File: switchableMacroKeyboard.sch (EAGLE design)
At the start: 36 parts

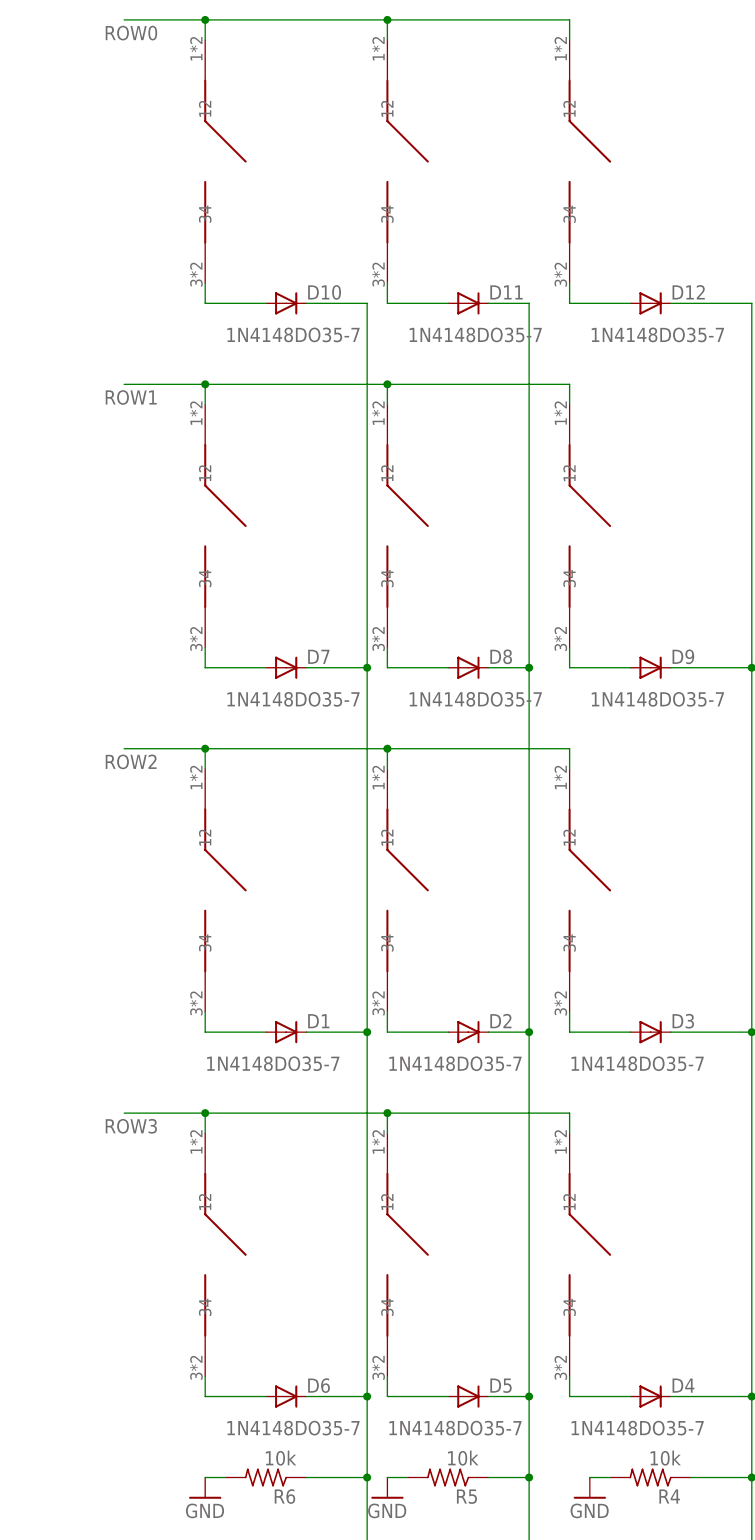
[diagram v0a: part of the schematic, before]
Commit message: Switched the buttons to Cherry MX Blues, but found this may require a bigger board, mostly length-wise. Moving the diodes out of the way of the key has cramped things. To do: adjust board dimensions to fit new buttons, reroute keypad traces.
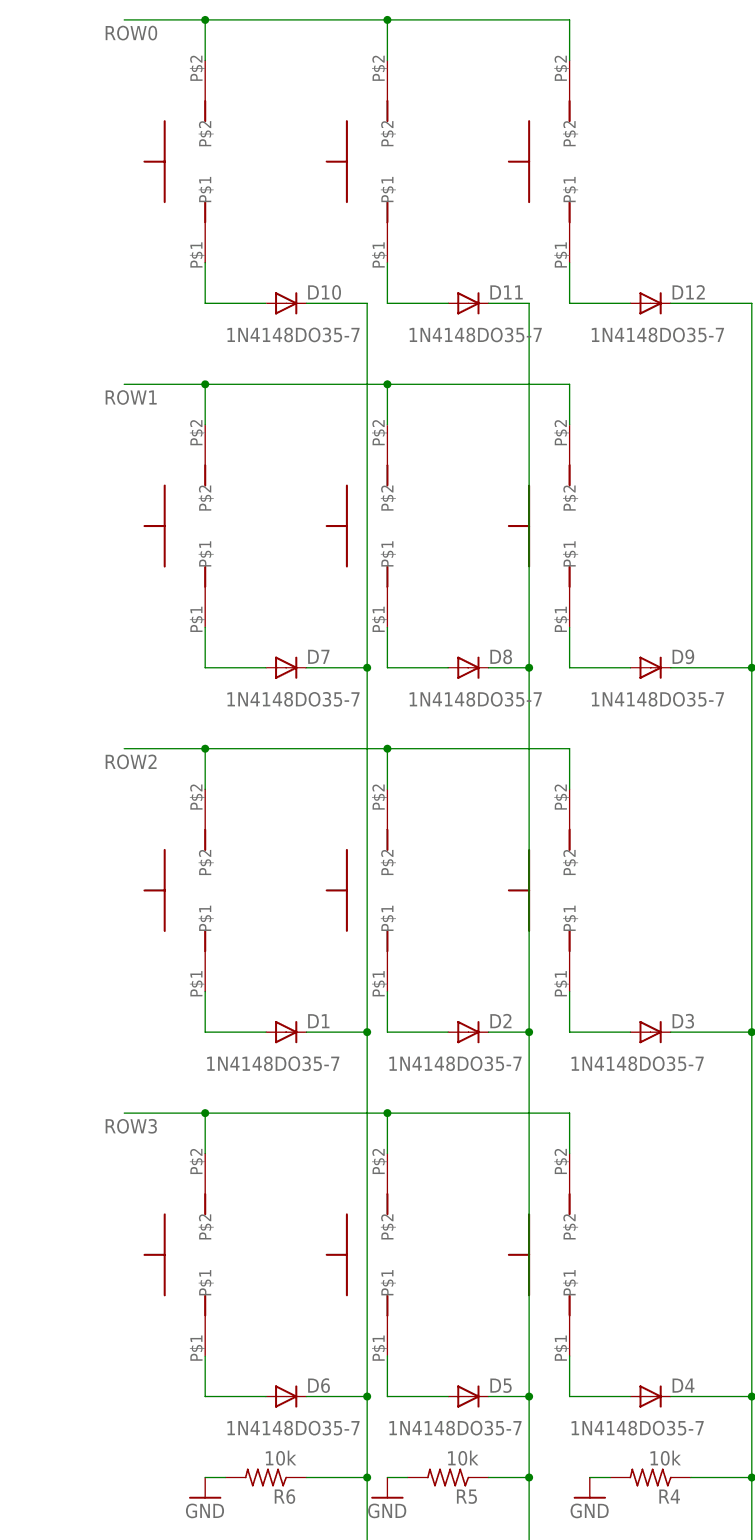
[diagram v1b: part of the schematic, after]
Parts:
- removed 00, 01, 02, 10, 11, 12, 20, 21, 22, 30, 31, 32: TACT-PTS526-SMG15-SMTR2-LFS, ARNEInput:TACT-PTS526-SMG15-SMTR2-LFS
- added U$10, U$11, U$12, U$14, U$15, U$16, U$4, U$5, U$6, U$7, U$8, U$9: CHERRYMXBLUE, ARNEInput:CHERRYMXBLUE
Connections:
- net N$18: now also U$7.P$1; no longer 10.34
- net N$19: now also U$8.P$1; no longer 11.34
- net N$20: now also U$9.P$1; no longer 12.34
- net N$25: now also U$4.P$1; no longer 00.34
- net N$26: now also U$5.P$1; no longer 01.34
- net N$27: now also U$6.P$1; no longer 02.34
- net N$3: now also U$10.P$1; no longer 20.34
- net N$4: now also U$11.P$1; no longer 21.34
- net N$5: now also U$12.P$1; no longer 22.34
- net N$6: now also U$14.P$1; no longer 30.34
- net N$7: now also U$15.P$1; no longer 31.34
- net N$8: now also U$16.P$1; no longer 32.34
- net ROW0: now also U$4.P$2, U$5.P$2, U$6.P$2; no longer 00.12, 01.12, 02.12
- net ROW1: now also U$7.P$2, U$8.P$2, U$9.P$2; no longer 10.12, 11.12, 12.12
- net ROW2: now also U$10.P$2, U$11.P$2, U$12.P$2; no longer 20.12, 21.12, 22.12
- net ROW3: now also U$14.P$2, U$15.P$2, U$16.P$2; no longer 30.12, 31.12, 32.12

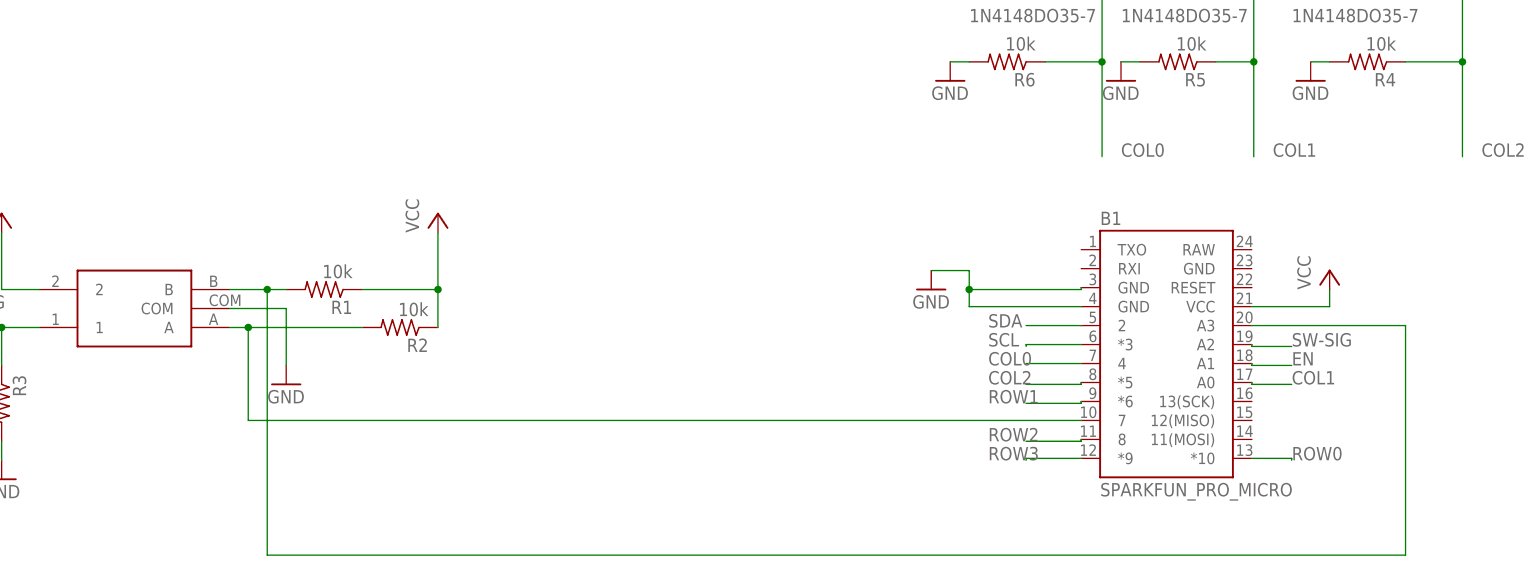
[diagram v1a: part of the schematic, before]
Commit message: Adjusted the size of the board and rerouted.
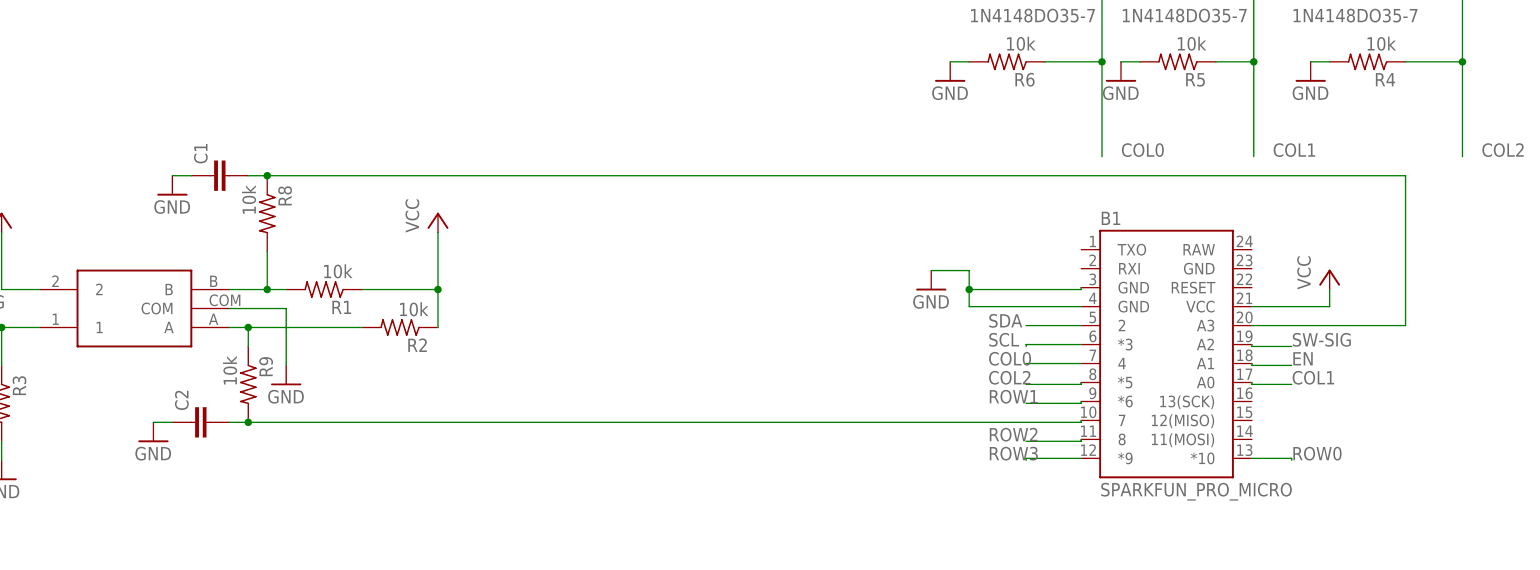
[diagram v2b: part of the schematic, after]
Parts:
- added C1, C2: (no value), capacitor-wima:C5/2.5
- added R8, R9: 10k, rcl:R-US_0207/10
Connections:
- new net N$10: R2.2, R9.1, U$13.A
- new net N$2: R1.2, R8.2, U$13.B
- net GND: now also C1.1, C2.1
- net N$1: now also C2.2, R9.2; no longer R2.2, U$13.A
- net N$9: now also C1.2, R8.1; no longer R1.2, U$13.B
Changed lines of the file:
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@@
 <part name="U$15" library="ARNEInput" deviceset="CHERRYMXBLUE" device=""/>
 <part name="U$16" library="ARNEInput" deviceset="CHERRYMXBLUE" device=""/>
+<part name="R8" library="rcl" library_urn="urn:adsk.eagle:library:334" deviceset="R-US_" device="0207/10" package3d_urn="urn:adsk.eagle:package:23491/2" value="10k"/>
+<part name="R9" library="rcl" library_urn="urn:adsk.eagle:library:334" deviceset="R-US_" device="0207/10" package3d_urn="urn:adsk.eagle:package:23491/2" value="10k"/>
+<part name="C1" library="capacitor-wima" library_urn="urn:adsk.eagle:library:116" deviceset="C" device="5/2.5" package3d_urn="urn:adsk.eagle:package:5426/1"/>
+<part name="C2" library="capacitor-wima" library_urn="urn:adsk.eagle:library:116" deviceset="C" device="5/2.5" package3d_urn="urn:adsk.eagle:package:5426/1"/>
+<part name="GND9" library="supply1" library_urn="urn:adsk.eagle:library:371" deviceset="GND" device=""/>
+<part name="GND10" library="supply1" library_urn="urn:adsk.eagle:library:371" deviceset="GND" device=""/>
 </parts>
 <sheets>
@@
 <instance part="U$15" gate="G$1" x="25.4" y="40.64" smashed="yes" rot="R90"/>
 <instance part="U$16" gate="G$1" x="48.26" y="40.64" smashed="yes" rot="R90"/>
+<instance part="R8" gate="G$1" x="-88.9" y="-7.62" smashed="yes" rot="R270">
+<attribute name="NAME" x="-87.4014" y="-3.81" size="1.778" layer="95" rot="R270"/>
+<attribute name="VALUE" x="-92.202" y="-3.81" size="1.778" layer="96" rot="R270"/>
+</instance>
+<instance part="R9" gate="G$1" x="-91.44" y="-30.48" smashed="yes" rot="R270">
+<attribute name="NAME" x="-89.9414" y="-26.67" size="1.778" layer="95" rot="R270"/>
+<attribute name="VALUE" x="-94.742" y="-26.67" size="1.778" layer="96" rot="R270"/>
+</instance>
+<instance part="C1" gate="G$1" x="-96.52" y="-2.54" smashed="yes" rot="R90">
+<attribute name="NAME" x="-96.901" y="-1.016" size="1.778" layer="95" rot="R90"/>
+<attribute name="VALUE" x="-91.821" y="-1.016" size="1.778" layer="96" rot="R90"/>
+</instance>
+<instance part="C2" gate="G$1" x="-99.06" y="-35.56" smashed="yes" rot="R90">
+<attribute name="NAME" x="-99.441" y="-34.036" size="1.778" layer="95" rot="R90"/>
+<attribute name="VALUE" x="-94.361" y="-34.036" size="1.778" layer="96" rot="R90"/>
+</instance>
+<instance part="GND9" gate="1" x="-104.14" y="-38.1" smashed="yes">
+<attribute name="VALUE" x="-106.68" y="-40.64" size="1.778" layer="96"/>
+</instance>
+<instance part="GND10" gate="1" x="-101.6" y="-5.08" smashed="yes">
+<attribute name="VALUE" x="-104.14" y="-7.62" size="1.778" layer="96"/>
+</instance>
 </instances>
 <busses>
@@
 <net name="N$9" class="0">
 <segment>
-<pinref part="R1" gate="G$1" pin="2"/>
-<pinref part="U$13" gate="G$1" pin="B"/>
-<wire x1="-86.36" y1="-17.78" x2="-88.9" y2="-17.78" width="0.1524" layer="91"/>
 <pinref part="B1" gate="G$1" pin="A3"/>
-<wire x1="-88.9" y1="-17.78" x2="-93.98" y2="-17.78" width="0.1524" layer="91"/>
 <wire x1="42.926" y1="-22.606" x2="63.5" y2="-22.606" width="0.1524" layer="91"/>
-<wire x1="63.5" y1="-22.606" x2="63.5" y2="-53.34" width="0.1524" layer="91"/>
-<wire x1="63.5" y1="-53.34" x2="-88.9" y2="-53.34" width="0.1524" layer="91"/>
-<wire x1="-88.9" y1="-53.34" x2="-88.9" y2="-17.78" width="0.1524" layer="91"/>
-<junction x="-88.9" y="-17.78"/>
+<wire x1="63.5" y1="-22.606" x2="63.5" y2="-2.54" width="0.1524" layer="91"/>
+<wire x1="63.5" y1="-2.54" x2="-88.9" y2="-2.54" width="0.1524" layer="91"/>
+<pinref part="R8" gate="G$1" pin="1"/>
+<pinref part="C1" gate="G$1" pin="2"/>
+<wire x1="-88.9" y1="-2.54" x2="-91.44" y2="-2.54" width="0.1524" layer="91"/>
+<junction x="-88.9" y="-2.54"/>
 </segment>
 </net>
@@
 <wire x1="91.44" y1="22.86" x2="86.36" y2="22.86" width="0.1524" layer="91"/>
 </segment>
+<segment>
+<pinref part="C1" gate="G$1" pin="1"/>
+<pinref part="GND10" gate="1" pin="GND"/>
+<wire x1="-99.06" y1="-2.54" x2="-101.6" y2="-2.54" width="0.1524" layer="91"/>
+</segment>
+<segment>
+<pinref part="C2" gate="G$1" pin="1"/>
+<pinref part="GND9" gate="1" pin="GND"/>
+<wire x1="-101.6" y1="-35.56" x2="-104.14" y2="-35.56" width="0.1524" layer="91"/>
+</segment>
 </net>
 <net name="SW-SIG" class="0">
@@
 <wire x1="101.6" y1="15.24" x2="106.68" y2="15.24" width="0.1524" layer="91"/>
 <label x="109.22" y="15.24" size="1.778" layer="95"/>
-</segment>
-</net>
-<net name="N$1" class="0">
-<segment>
-<pinref part="U$13" gate="G$1" pin="A"/>
-<pinref part="R2" gate="G$1" pin="2"/>
-<wire x1="-76.2" y1="-22.86" x2="-91.44" y2="-22.86" width="0.1524" layer="91"/>
-<pinref part="B1" gate="G$1" pin="7"/>
-<wire x1="-91.44" y1="-22.86" x2="-93.98" y2="-22.86" width="0.1524" layer="91"/>
-<wire x1="20.066" y1="-35.306" x2="-91.44" y2="-35.306" width="0.1524" layer="91"/>
-<wire x1="-91.44" y1="-35.306" x2="-91.44" y2="-22.86" width="0.1524" layer="91"/>
-<junction x="-91.44" y="-22.86"/>
 </segment>
 </net>
@@
 </segment>
 </net>
+<net name="N$2" class="0">
+<segment>
+<pinref part="U$13" gate="G$1" pin="B"/>
+<pinref part="R1" gate="G$1" pin="2"/>
+<wire x1="-86.36" y1="-17.78" x2="-88.9" y2="-17.78" width="0.1524" layer="91"/>
+<pinref part="R8" gate="G$1" pin="2"/>
+<wire x1="-88.9" y1="-17.78" x2="-93.98" y2="-17.78" width="0.1524" layer="91"/>
+<wire x1="-88.9" y1="-12.7" x2="-88.9" y2="-17.78" width="0.1524" layer="91"/>
+<junction x="-88.9" y="-17.78"/>
+</segment>
+</net>
+<net name="N$10" class="0">
+<segment>
+<pinref part="U$13" gate="G$1" pin="A"/>
+<pinref part="R2" gate="G$1" pin="2"/>
+<wire x1="-76.2" y1="-22.86" x2="-91.44" y2="-22.86" width="0.1524" layer="91"/>
+<pinref part="R9" gate="G$1" pin="1"/>
+<wire x1="-91.44" y1="-22.86" x2="-93.98" y2="-22.86" width="0.1524" layer="91"/>
+<wire x1="-91.44" y1="-25.4" x2="-91.44" y2="-22.86" width="0.1524" layer="91"/>
+<junction x="-91.44" y="-22.86"/>
+</segment>
+</net>
+<net name="N$1" class="0">
+<segment>
+<pinref part="B1" gate="G$1" pin="7"/>
+<pinref part="R9" gate="G$1" pin="2"/>
+<wire x1="20.066" y1="-35.306" x2="20.066" y2="-35.56" width="0.1524" layer="91"/>
+<wire x1="20.066" y1="-35.56" x2="-91.44" y2="-35.56" width="0.1524" layer="91"/>
+<pinref part="C2" gate="G$1" pin="2"/>
+<wire x1="-91.44" y1="-35.56" x2="-93.98" y2="-35.56" width="0.1524" layer="91"/>
+<junction x="-91.44" y="-35.56"/>
+</segment>
+</net>
